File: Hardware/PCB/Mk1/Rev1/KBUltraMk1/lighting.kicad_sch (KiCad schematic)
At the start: 181 parts

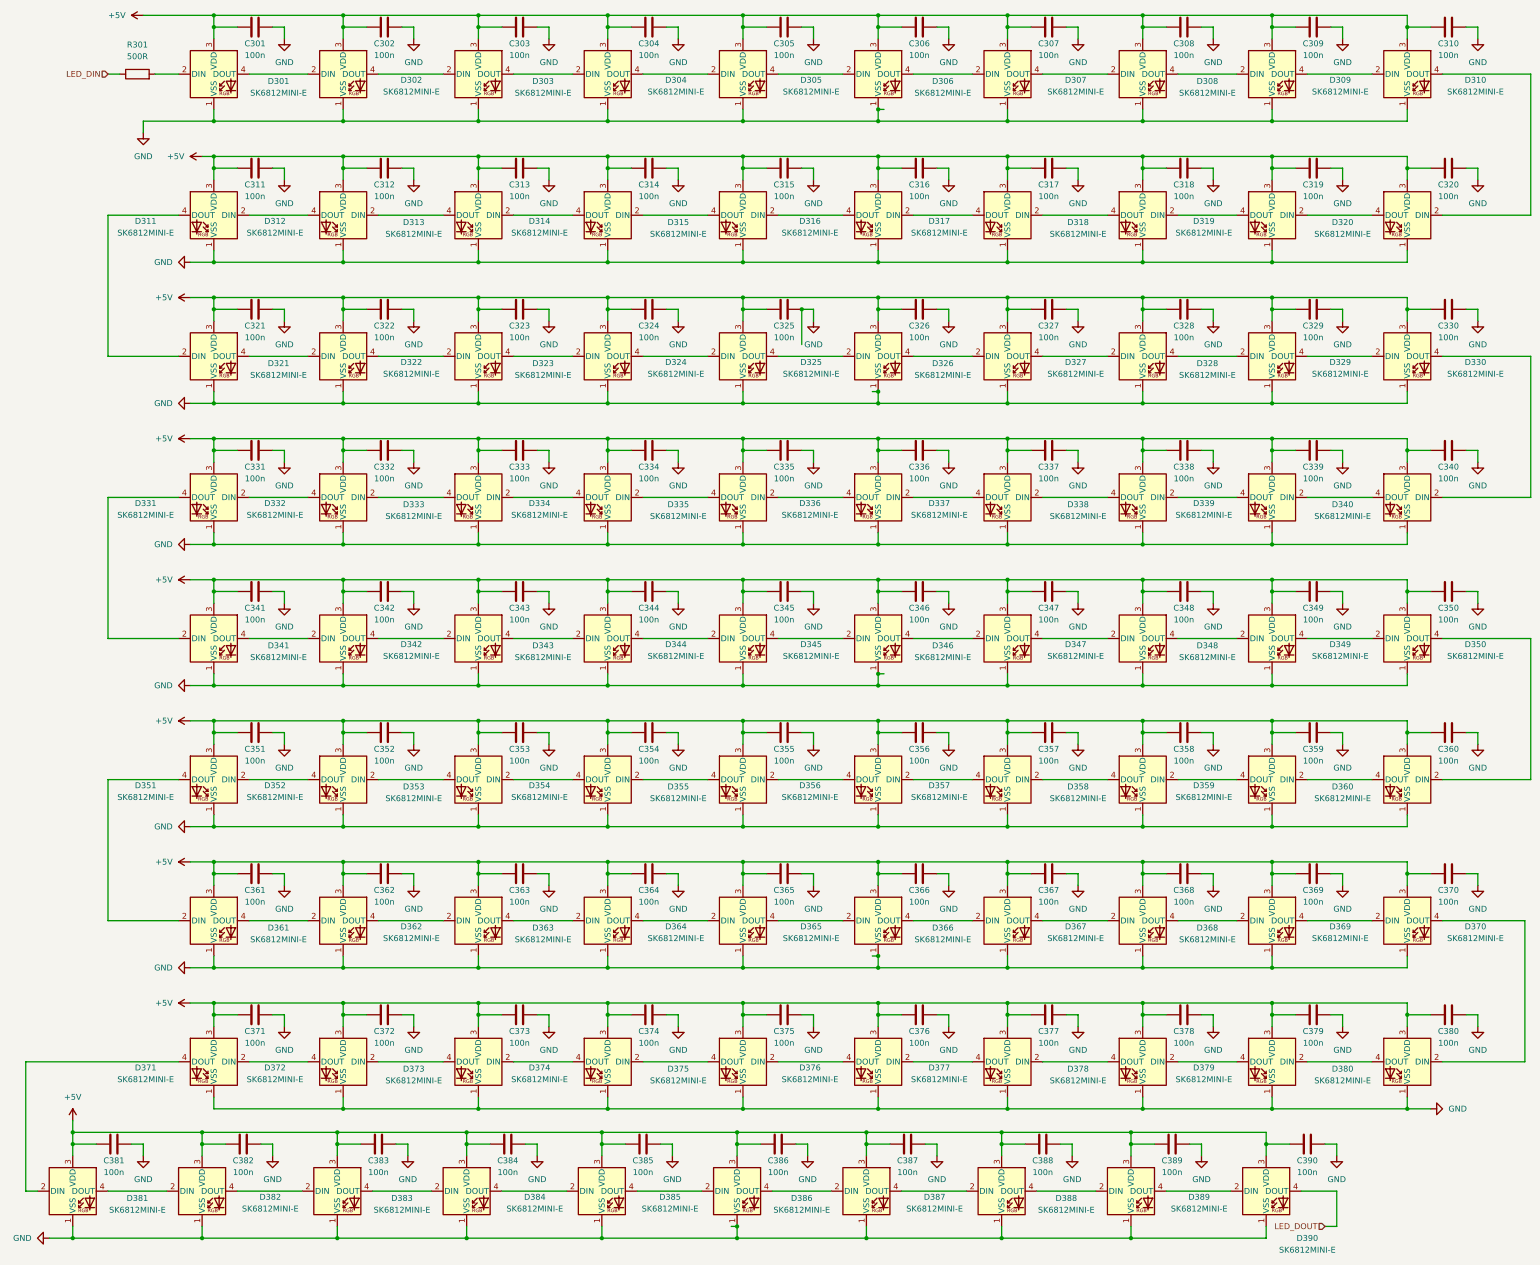
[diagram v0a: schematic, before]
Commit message: Added RP MCU
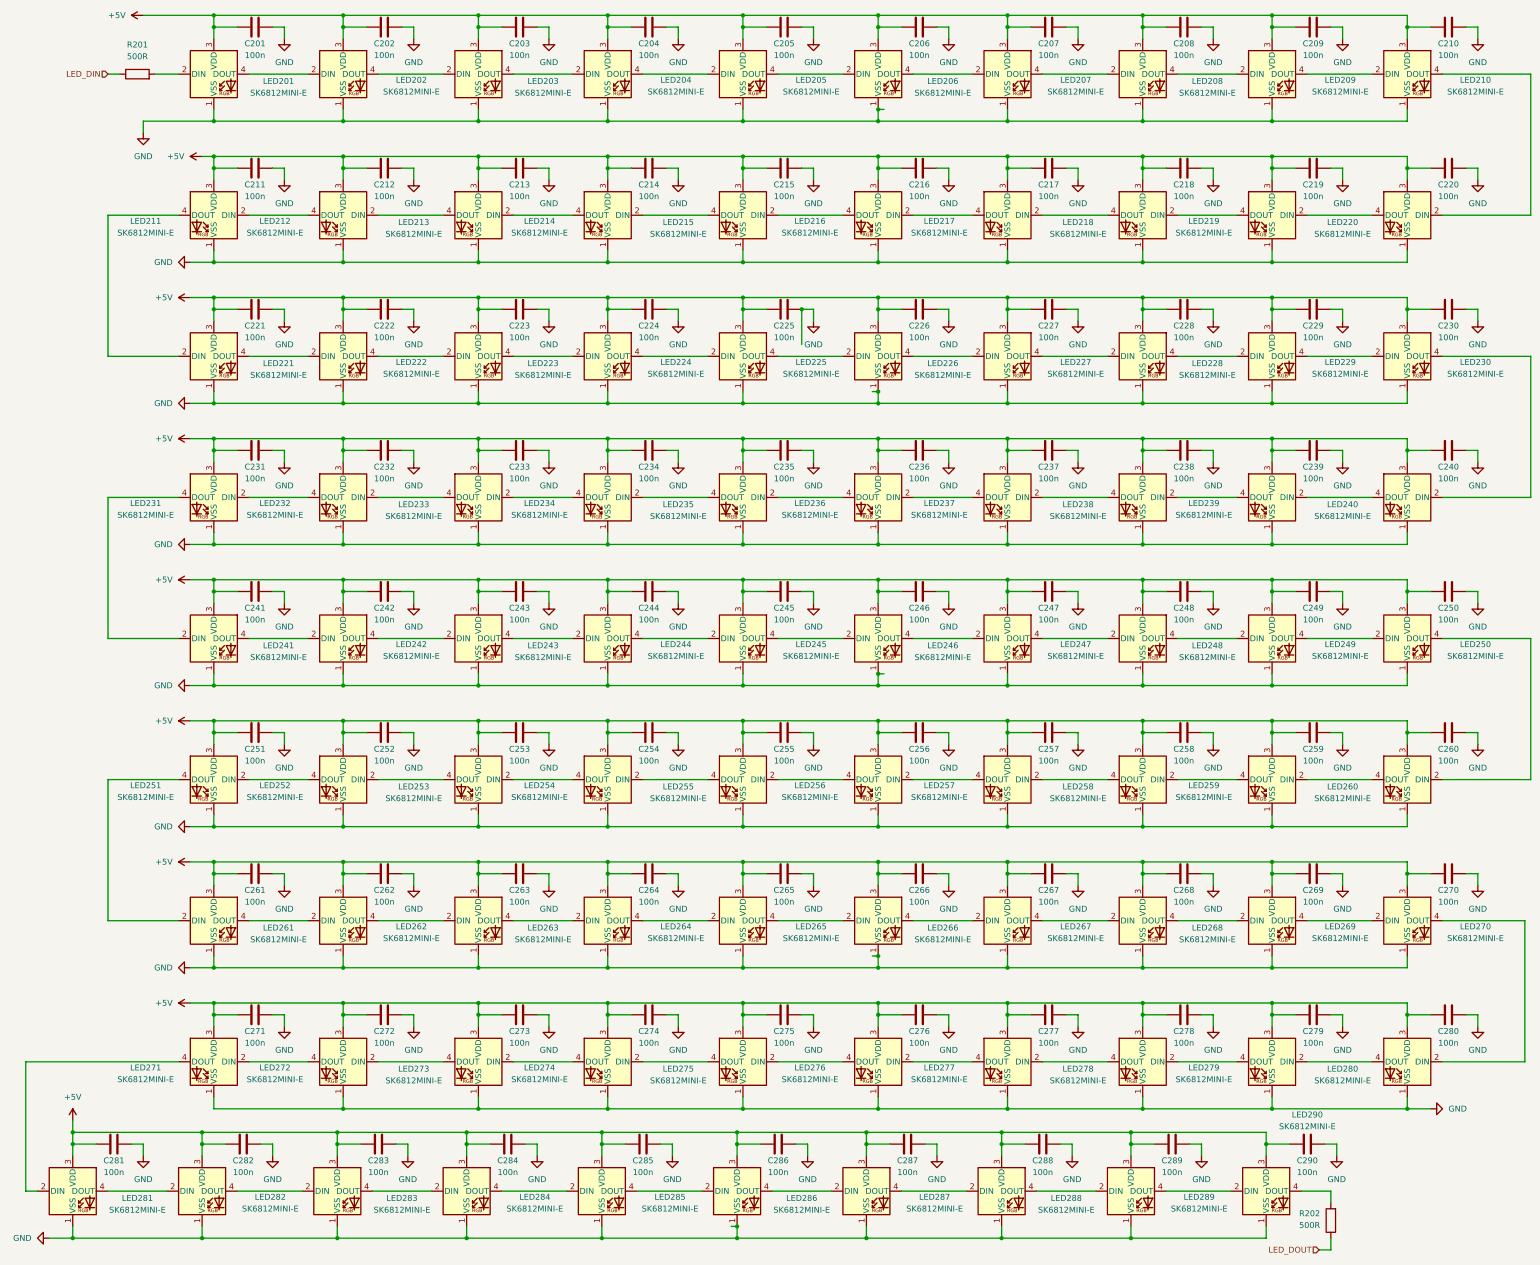
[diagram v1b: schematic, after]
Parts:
- added R202: 500R, Resistor_SMD:R_0603_1608Metric, symbol Device:R
- renumbered C301 to C201, C302 to C202, C303 to C203, C304 to C204, C305 to C205, C306 to C206, C307 to C207, C308 to C208, C309 to C209, C310 to C210, C311 to C211, C312 to C212, C313 to C213, C314 to C214, C315 to C215, C316 to C216, C317 to C217, C318 to C218, C319 to C219, C320 to C220, C321 to C221, C322 to C222, C323 to C223, C324 to C224, C325 to C225, C326 to C226, C327 to C227, C328 to C228, C329 to C229, C330 to C230, C331 to C231, C332 to C232, C333 to C233, C334 to C234, C335 to C235, C336 to C236, C337 to C237, C338 to C238, C339 to C239, C340 to C240, C341 to C241, C342 to C242, C343 to C243, C344 to C244, C345 to C245, C346 to C246, C347 to C247, C348 to C248, C349 to C249, C350 to C250, C351 to C251, C352 to C252, C353 to C253, C354 to C254, C355 to C255, C356 to C256, C357 to C257, C358 to C258, C359 to C259, C360 to C260, C361 to C261, C362 to C262, C363 to C263, C364 to C264, C365 to C265, C366 to C266, C367 to C267, C368 to C268, C369 to C269, C370 to C270, C371 to C271, C372 to C272, C373 to C273, C374 to C274, C375 to C275, C376 to C276, C377 to C277, C378 to C278, C379 to C279, C380 to C280, C381 to C281, C382 to C282, C383 to C283, C384 to C284, C385 to C285, C386 to C286, C387 to C287, C388 to C288, C389 to C289, C390 to C290, D301 to LED201, D302 to LED202, D303 to LED203, D304 to LED204, D305 to LED205, D306 to LED206, D307 to LED207, D308 to LED208, D309 to LED209, D310 to LED210, D311 to LED211, D312 to LED212, D313 to LED213, D314 to LED214, D315 to LED215, D316 to LED216, D317 to LED217, D318 to LED218, D319 to LED219, D320 to LED220, D321 to LED221, D322 to LED222, D323 to LED223, D324 to LED224, D325 to LED225, D326 to LED226, D327 to LED227, D328 to LED228, D329 to LED229, D330 to LED230, D331 to LED231, D332 to LED232, D333 to LED233, D334 to LED234, D335 to LED235, D336 to LED236, D337 to LED237, D338 to LED238, D339 to LED239, D340 to LED240, D341 to LED241, D342 to LED242, D343 to LED243, D344 to LED244, D345 to LED245, D346 to LED246, D347 to LED247, D348 to LED248, D349 to LED249, D350 to LED250, D351 to LED251, D352 to LED252, D353 to LED253, D354 to LED254, D355 to LED255, D356 to LED256, D357 to LED257, D358 to LED258, D359 to LED259, D360 to LED260, D361 to LED261, D362 to LED262, D363 to LED263, D364 to LED264, D365 to LED265, D366 to LED266, D367 to LED267, D368 to LED268, D369 to LED269, D370 to LED270, D371 to LED271, D372 to LED272, D373 to LED273, D374 to LED274, D375 to LED275, D376 to LED276, D377 to LED277, D378 to LED278, D379 to LED279, D380 to LED280, D381 to LED281, D382 to LED282, D383 to LED283, D384 to LED284, D385 to LED285, D386 to LED286, D387 to LED287, D388 to LED288, D389 to LED289, D390 to LED290, R301 to R201
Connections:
- net LED_DOUT: now also R202.1; no longer LED290.4 (DOUT)
- new net: LED290.4 (DOUT), R202.2

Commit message: A
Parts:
- removed C276, C277, C278, C280, C282, C289, C290: 100n, Capacitor_SMD:C_0603_1608Metric, symbol Device:C
- removed LED276, LED277, LED278, LED280, LED282, LED289, LED290: SK6812MINI-E, LED_SMD:LED_SK6812MINI-E_3.2x2.8mm_P1.5mm_ReverseMount, symbol LED:SK6812MINI-E
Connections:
- net at LED275.2 (DIN): now also LED279.4 (DOUT)
- net at LED288.4 (DOUT): now also R202.2
- net at LED270.4 (DOUT): now also LED279.2 (DIN)
- net at LED281.4 (DOUT): now also LED283.2 (DIN)
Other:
- moved on the sheet: C279, R202

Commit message: A:
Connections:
- net at LED258.2 (DIN): now also LED257.4 (DOUT); no longer LED259.4 (DOUT)
- net at LED258.4 (DOUT): now also LED259.2 (DIN); no longer LED257.2 (DIN)
- net at LED254.2 (DIN): now also LED253.4 (DOUT); no longer LED255.4 (DOUT)
- net at LED254.4 (DOUT): now also LED255.2 (DIN); no longer LED253.2 (DIN)
- net at LED271.2 (DIN): now also LED270.4 (DOUT); no longer LED272.4 (DOUT)
- net at LED271.4 (DOUT): now also LED272.2 (DIN); no longer LED281.2 (DIN)
- net at LED237.2 (DIN): now also LED236.4 (DOUT); no longer LED238.4 (DOUT)
- net at LED237.4 (DOUT): now also LED238.2 (DIN); no longer LED236.2 (DIN)
- net at LED231.2 (DIN): now also LED230.4 (DOUT); no longer LED232.4 (DOUT)
- net at LED231.4 (DOUT): now also LED232.2 (DIN); no longer LED241.2 (DIN)
- net at LED213.2 (DIN): now also LED212.4 (DOUT); no longer LED214.4 (DOUT)
- net at LED213.4 (DOUT): now also LED214.2 (DIN); no longer LED212.2 (DIN)
- net at LED217.2 (DIN): now also LED216.4 (DOUT); no longer LED218.4 (DOUT)
- net at LED217.4 (DOUT): now also LED218.2 (DIN); no longer LED216.2 (DIN)
- net at LED240.2 (DIN): now also LED239.4 (DOUT); no longer LED230.4 (DOUT)
- net at LED235.2 (DIN): now also LED234.4 (DOUT); no longer LED236.4 (DOUT)
- net at LED251.2 (DIN): now also LED250.4 (DOUT); no longer LED252.4 (DOUT)
- net at LED251.4 (DOUT): now also LED252.2 (DIN); no longer LED261.2 (DIN)
- net at LED260.4 (DOUT): now also LED261.2 (DIN); no longer LED259.2 (DIN)
- net at LED279.2 (DIN): now also LED275.4 (DOUT); no longer LED270.4 (DOUT)
- net at LED239.2 (DIN): now also LED238.4 (DOUT); no longer LED240.4 (DOUT)
- net at LED235.4 (DOUT): now also LED236.2 (DIN); no longer LED234.2 (DIN)
- net at LED211.2 (DIN): now also LED210.4 (DOUT); no longer LED212.4 (DOUT)
- net at LED279.4 (DOUT): now also LED281.2 (DIN); no longer LED275.2 (DIN)
- net at LED233.2 (DIN): now also LED232.4 (DOUT); no longer LED234.4 (DOUT)
- net at LED233.4 (DOUT): now also LED234.2 (DIN); no longer LED232.2 (DIN)
- net at LED215.2 (DIN): now also LED214.4 (DOUT); no longer LED216.4 (DOUT)
- net at LED215.4 (DOUT): now also LED216.2 (DIN); no longer LED214.2 (DIN)
- net at LED273.2 (DIN): now also LED272.4 (DOUT); no longer LED274.4 (DOUT)
- net at LED273.4 (DOUT): now also LED274.2 (DIN); no longer LED272.2 (DIN)
- net at LED256.2 (DIN): now also LED255.4 (DOUT); no longer LED257.4 (DOUT)
- net at LED256.4 (DOUT): now also LED257.2 (DIN); no longer LED255.2 (DIN)
- net at LED220.2 (DIN): now also LED219.4 (DOUT); no longer LED210.4 (DOUT)
- net at LED260.2 (DIN): now also LED259.4 (DOUT); no longer LED250.4 (DOUT)
- net at LED211.4 (DOUT): now also LED212.2 (DIN); no longer LED221.2 (DIN)
- net at LED219.2 (DIN): now also LED218.4 (DOUT); no longer LED220.4 (DOUT)
- new net: LED240.4 (DOUT), LED241.2 (DIN)
- new net: LED252.4 (DOUT), LED253.2 (DIN)
- new net: LED274.4 (DOUT), LED275.2 (DIN)
- new net: LED220.4 (DOUT), LED221.2 (DIN)
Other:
- moved on the sheet: C281, C283, C284, C285, C286, C287, C288, LED281, LED283, LED284, LED285, LED286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
